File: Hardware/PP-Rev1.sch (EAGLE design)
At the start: 178 parts, among them IC1 LT6004, IC2 TLC6C5912-Q1, Q1 MOSFET-PCHANNEL, Q10 2N7002PW, Q11 2N7002PW, Q12 2N7002PW, Q13 2N7002PW, Q14 2N7002PW, Q15 2N7002PW, Q2 MOSFET-PCHANNEL, Q3 MOSFET-PCHANNEL, Q4 MOSFET-PCHANNEL, Q5 MOSFET-PCHANNEL, Q6 MOSFET-PCHANNEL, Q7 MOSFET-PCHANNEL, Q8 MOSFET-PCHANNEL, Q9 CSD18532, U1 WIZ811MJ, X1 22-23-2031, X2 22-23-2031, X3 22-23-2031, X4 22-23-2031

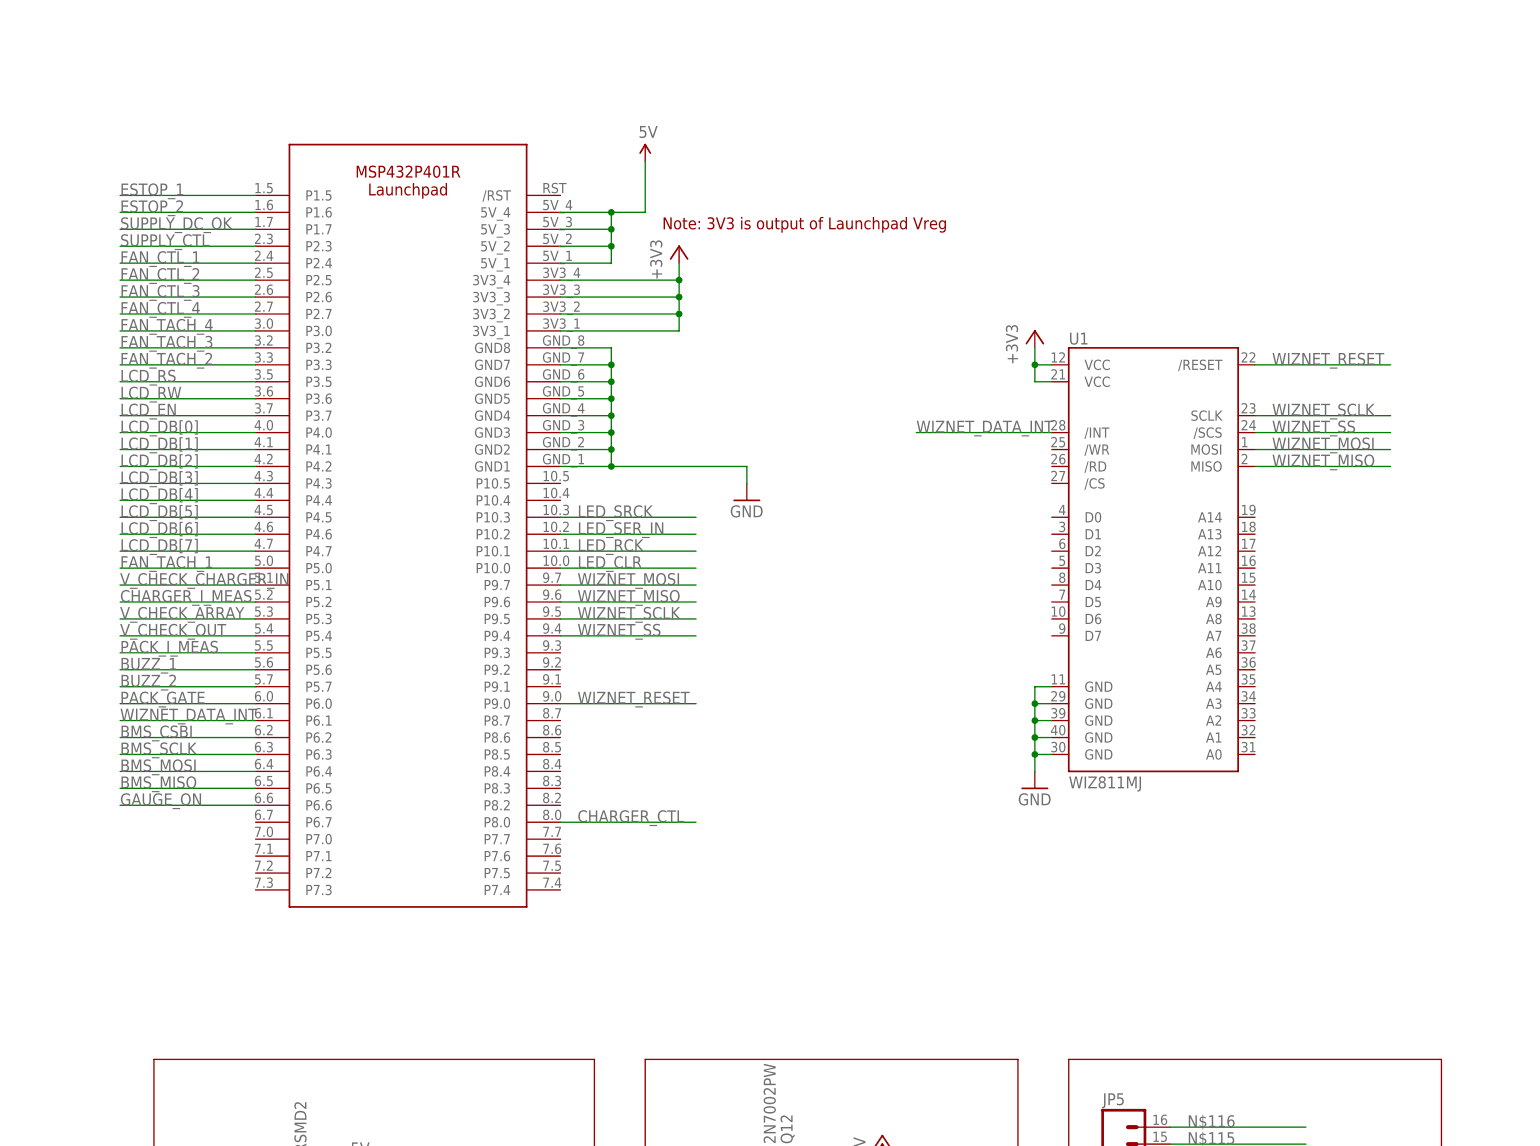
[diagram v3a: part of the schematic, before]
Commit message: Minor schematic formatting cleanup
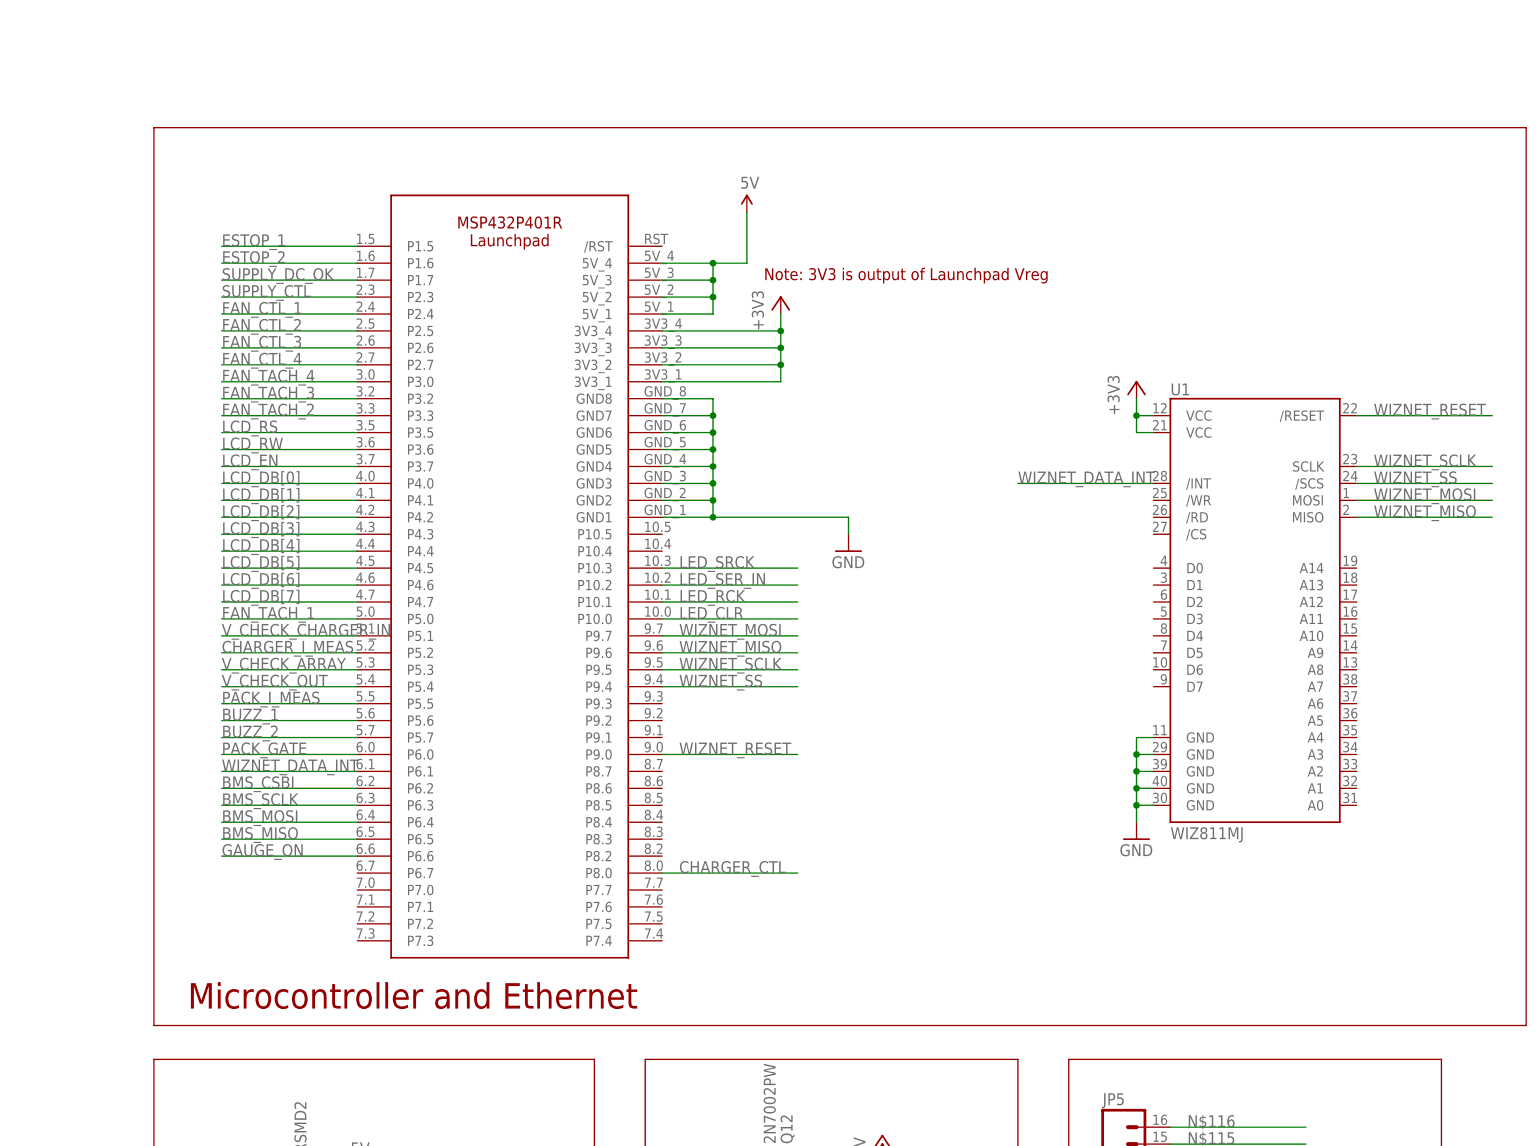
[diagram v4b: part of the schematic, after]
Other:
- note added: "Microcontroller and Ethernet"
- moved on the sheet: U1

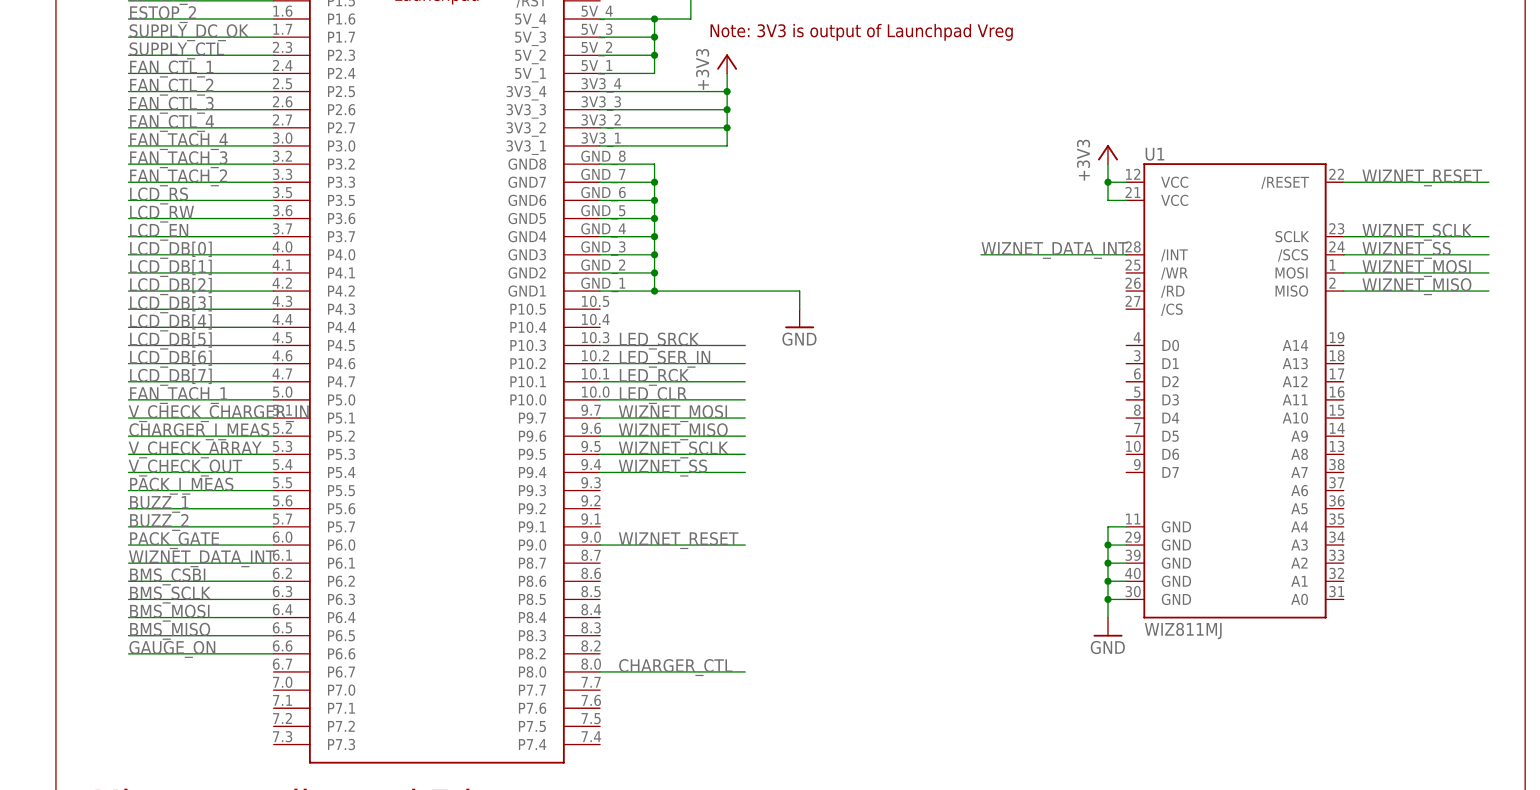
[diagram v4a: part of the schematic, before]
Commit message: Changed from Ethernet to RS485 to communciate to power board
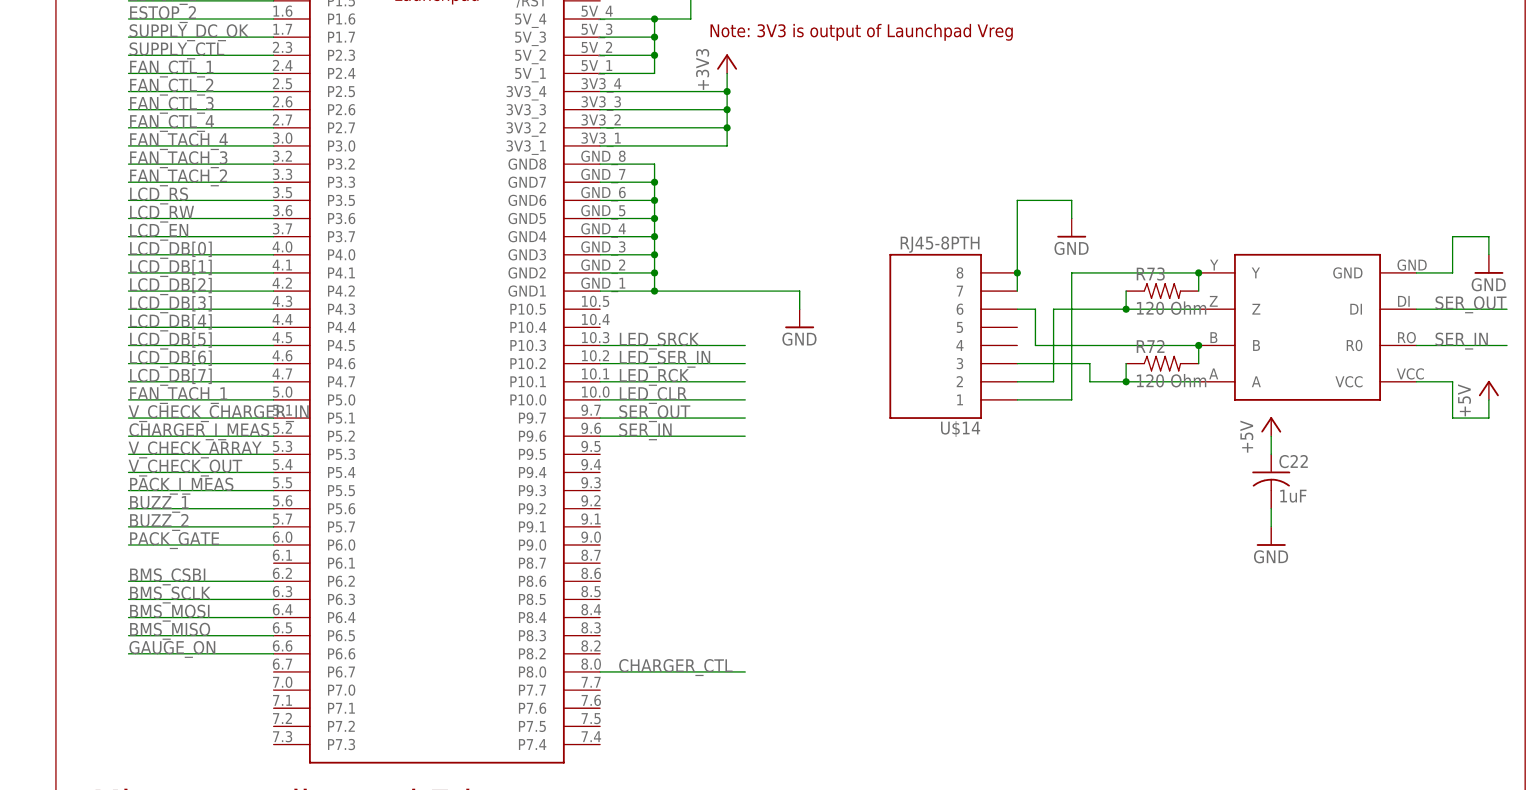
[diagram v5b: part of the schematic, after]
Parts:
- removed U1: WIZ811MJ, SparkFun-Boards:WIZ811MJ
- added C22: 1uF, resistor:C-USC1206
- added R72, R73: 120 Ohm, SparkFun-Passives:RESISTOR1206
- added U$14: RJ45-8PTH, SparkFun-Connectors:RJ45-8PTH
- added U$15: MAX3077, MAX3077:MAX3077
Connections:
- removed net WIZNET_DATA_INT: U$13.P6.1, U1./INT
- removed net WIZNET_MISO: U$13.P9.6, U1.MISO
- removed net WIZNET_MOSI: U$13.P9.7, U1.MOSI
- removed net WIZNET_RESET: U$13.P9.0, U1./RESET
- removed net WIZNET_SCLK: U$13.P9.5, U1.SCLK
- removed net WIZNET_SS: U$13.P9.4, U1./SCS
- new net N$35: R73.2, U$14.1, U$15.Y
- new net N$45: R73.1, U$14.2, U$15.Z
- new net N$62: R72.2, U$14.6, U$15.B
- new net N$67: R72.1, U$14.3, U$15.A
- new net SER_IN: U$13.P9.6, U$15.R0
- new net SER_OUT: U$13.P9.7, U$15.DI
- net +3V3: no longer U1.VCC@1, U1.VCC@2
- net +5V: now also C22.1, U$15.VCC
- net GND: now also C22.2, U$14.7, U$14.8, U$15.GND; no longer U1.GND@1, U1.GND@2, U1.GND@3, U1.GND@4, U1.GND@5
